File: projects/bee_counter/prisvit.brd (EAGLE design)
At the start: 20.3 x 36.5 mm, 5 parts

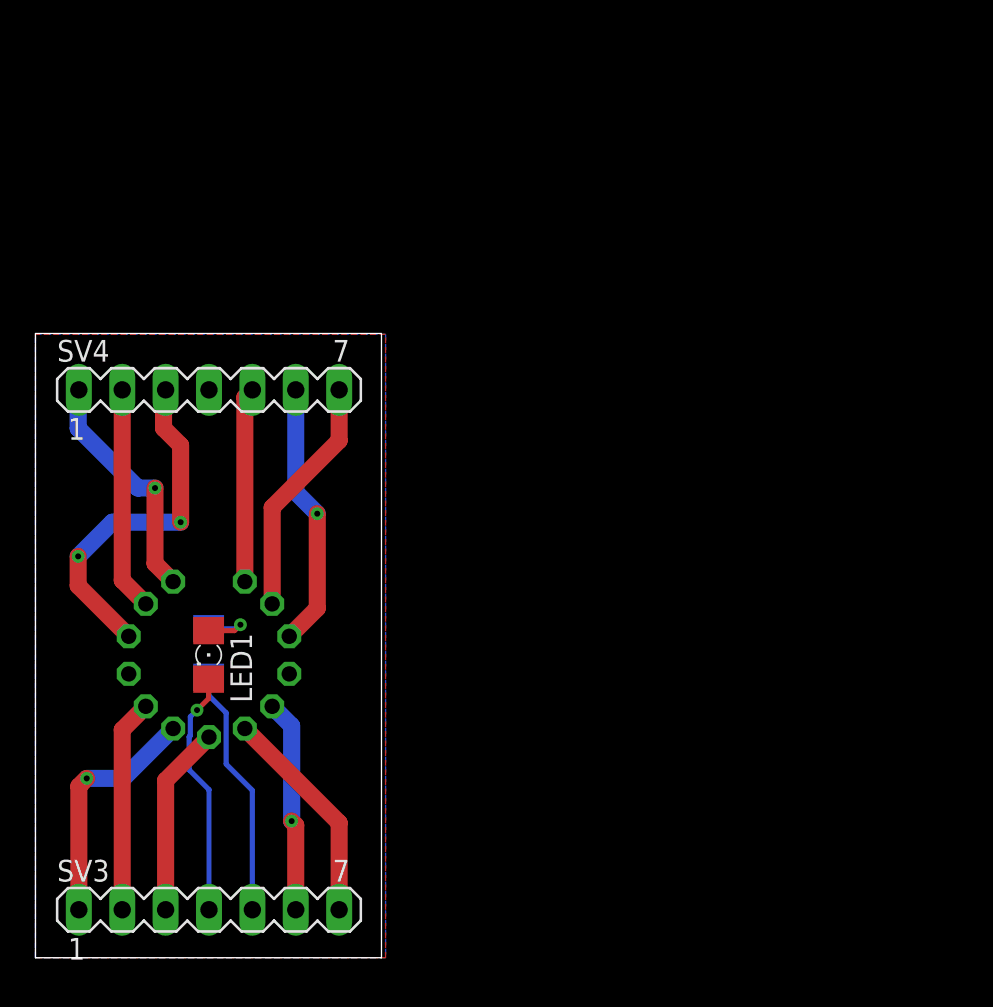
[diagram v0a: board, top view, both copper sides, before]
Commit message: added bee counter light
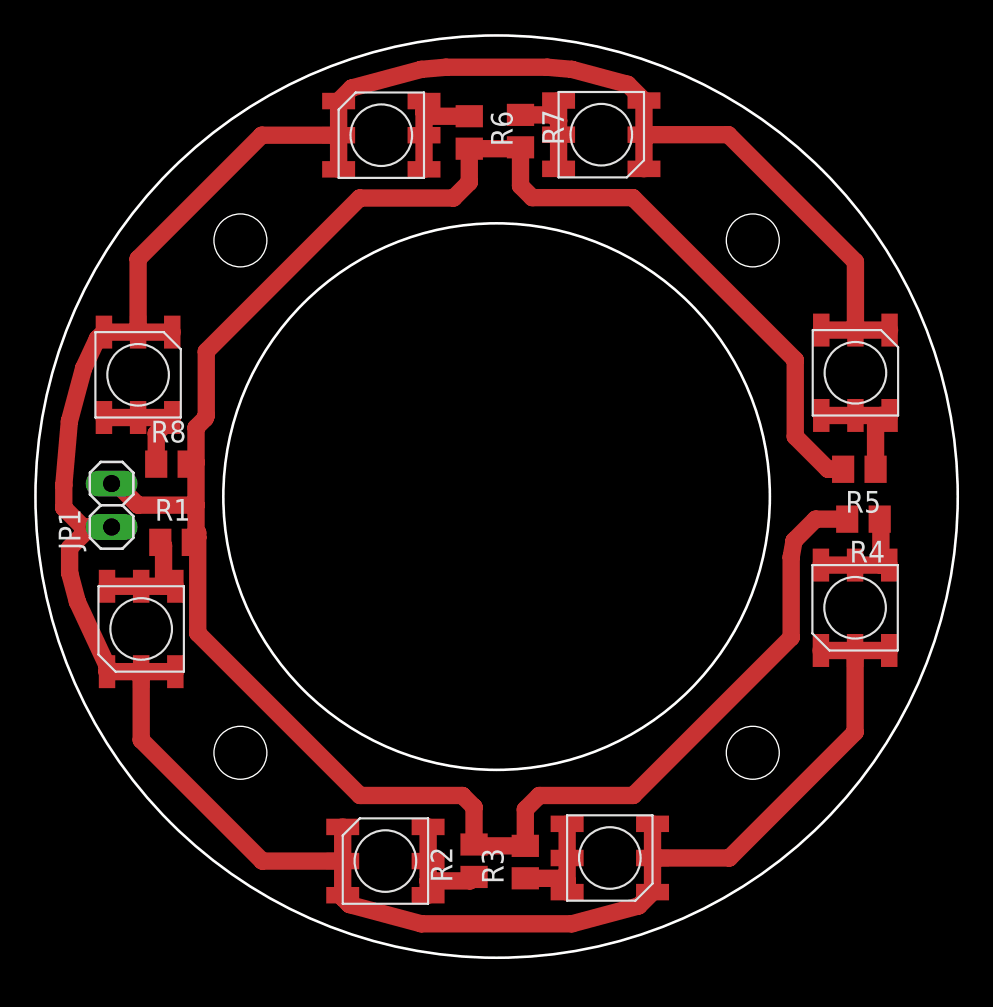
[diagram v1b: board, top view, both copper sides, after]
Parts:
- removed LED1: (no value), led:1206
- removed SV3, SV4: (no value), con-lstb:MA07-1
- added JP1: (no value), pinhead:1X02
- added R2, R3, R4, R5, R6, R7, R8: (no value), rcl:M2012
- added U$1, U$3, U$4, U$5, U$6, U$7, U$8: 5050_LED, leds:5050_LED
- R1: device rcl:R1206 -> rcl:M2012
- U$2: value ZM_1080 -> 5050_LED; device zm_1080:ZM_1080 -> leds:5050_LED
- moved R1 6.75 mm to (8.26, 24.3), flipped to the top, turned to 0 degrees
- moved U$2 4.25 mm to (6.19, 19.2), flipped to the top, turned to 90 degrees
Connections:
- removed net 0: SV4.7, U$2.K0
- removed net 1: SV4.1, U$2.K1
- removed net 2: SV4.2, U$2.K2
- removed net 3: SV4.3, U$2.K3
- removed net 4: SV3.2, U$2.K4
- removed net 5: SV3.1, U$2.K5
- removed net 5V: R1.2, SV3.5
- removed net 6: SV3.3, U$2.K6
- removed net 7: SV3.7, U$2.K7
- removed net 8: SV3.6, U$2.K8
- removed net 9: SV4.6, U$2.K9
- removed net A: SV4.5, U$2.A
- removed net N$13: SV4.4
- new net N$2: R4.1, U$6.1, U$6.3, U$6.5
- new net N$3: R3.1, U$4.1, U$4.3, U$4.5
- new net N$4: R2.1, U$3.1, U$3.3, U$3.5
- new net N$5: R1.1, U$2.1, U$2.3, U$2.5
- new net N$6: R5.1, U$8.1, U$8.3, U$8.5
- new net N$7: R7.1, U$1.1, U$1.3, U$1.5
- new net N$8: R6.1, U$5.1, U$5.3, U$5.5
- new net N$9: R8.1, U$7.1, U$7.3, U$7.5
- net GND: now also JP1.1, U$1.2, U$1.4, U$1.6, U$2.2, U$2.4, U$2.6, U$3.2, U$3.4, U$3.6, U$4.2, U$4.4, U$4.6, U$5.2, U$5.4, U$5.6, U$6.2, U$6.4, U$6.6, U$7.2, U$7.4, U$7.6, U$8.2, U$8.4, U$8.6; no longer LED1.C, SV3.4
- net N$1: now also JP1.2, R1.2, R2.2, R3.2, R4.2, R5.2, R6.2, R7.2, R8.2; no longer LED1.A, R1.1
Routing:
- net GND: track 14.5 -> 171.5 mm, vias 1 -> 0
- net N$1: track 3.96 -> 135.1 mm, vias 1 -> 0
- net 3: track 20.9 -> 0.00 mm, vias 2 -> 0
- net 9: track 15.6 -> 0.00 mm, vias 1 -> 0
- net 5V: track 14.7 -> 0.00 mm
- net 0: track 14.2 -> 0.00 mm
- net 5: track 14.2 -> 0.00 mm, vias 1 -> 0
- net 1: track 14.1 -> 0.00 mm, vias 1 -> 0
- net 2: track 13.1 -> 0.00 mm
- net 7: track 12.9 -> 0.00 mm
- net 8: track 12.5 -> 0.00 mm, vias 1 -> 0
- net 4: track 12.5 -> 0.00 mm
- net A: track 11.4 -> 0.00 mm
- net 6: track 11.2 -> 0.00 mm
- net N$6: track 0.00 -> 7.28 mm
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- removed copper zone on layer 1, net N$2
- removed copper zone on layer 16, net N$3
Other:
- board size 20.3 x 36.5 mm -> 54 x 54 mm
